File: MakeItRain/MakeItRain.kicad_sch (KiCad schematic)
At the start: 16 parts, among them IC1 MCP23008T-E_SS, J1 Conn_02x14_Odd_Even, J2 Conn_02x19_Odd_Even, J3 Conn_01x19, U1 MCP23008-xP

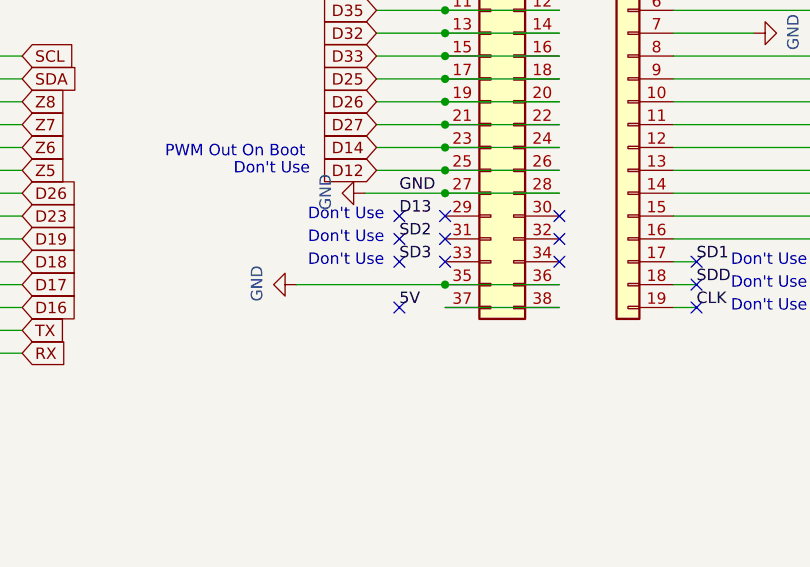
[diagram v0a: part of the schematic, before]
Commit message: in the process of cleaning up the HardwareValidation.ino and fixing a major fuck up for the board. misread a pin header.
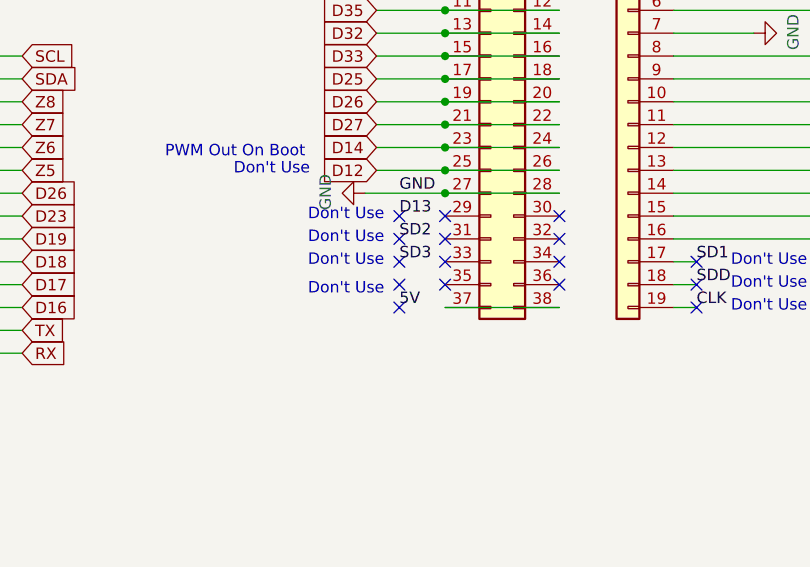
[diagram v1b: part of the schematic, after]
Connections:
- net GND: no longer J2.35 (Pin_35), J2.36 (Pin_36)
- no-connect marks 19 -> 22
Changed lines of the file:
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@@
 (kicad_sch (version 20211123) (generator eeschema)
   (paper "A4")
-  (junction (at 220.98 146.05) (diameter 0) (color 0 0 0 0)
-  )
   (junction (at 142.24 146.05) (diameter 0) (color 0 0 0 0)
   )
@@
   (no_connect (at 233.68 140.97))
   (no_connect (at 233.68 143.51))
+  (no_connect (at 215.9 146.05))
+  (no_connect (at 233.68 146.05))
   (no_connect (at 248.92 148.59))
+  (no_connect (at 220.98 146.05))
   (wire (pts (xy 90.17 142.875) (xy 92.71 142.875))
     (stroke (width 0) (type default) (color 0 0 0 0))
@@
     (stroke (width 0) (type default) (color 0 0 0 0))
   )
-  (wire (pts (xy 220.98 146.05) (xy 233.68 146.05))
-    (stroke (width 0) (type default) (color 0 0 0 0))
-  )
   (wire (pts (xy 90.17 125.095) (xy 92.71 125.095))
     (stroke (width 0) (type default) (color 0 0 0 0))
@@
   )
   (wire (pts (xy 233.68 107.95) (xy 220.98 107.95))
-    (stroke (width 0) (type default) (color 0 0 0 0))
-  )
-  (wire (pts (xy 204.47 146.05) (xy 220.98 146.05))
     (stroke (width 0) (type default) (color 0 0 0 0))
   )
@@
   )
   (text "Don't Use" (at 252.73 144.145 0)
+    (effects (font (size 1.27 1.27)) (justify left bottom))
+  )
+  (text "Don't Use" (at 205.74 147.32 0)
     (effects (font (size 1.27 1.27)) (justify left bottom))
   )
@@
     (pin "1")
   )
-  (symbol (lib_id "power:GND") (at 204.47 146.05 270) (mirror x) (unit 1)
-    (in_bom yes) (on_board yes)
-    (property "Reference" "#PWR0103" (id 0) (at 198.12 146.05 0)
-      (effects (font (size 1.27 1.27)) hide)
-    )
-    (property "Value" "GND" (id 1) (at 200.0758 145.923 0))
-    (property "Footprint" "" (id 2) (at 204.47 146.05 0)
-      (effects (font (size 1.27 1.27)) hide)
-    )
-    (property "Datasheet" "" (id 3) (at 204.47 146.05 0)
-      (effects (font (size 1.27 1.27)) hide)
-    )
-    (pin "1")
-  )
   (symbol (lib_id "Device:R") (at 35.56 116.84 0) (unit 1)
     (in_bom yes) (on_board yes)
@@
       (reference "#PWR0102") (unit 1) (value "+3.3V") (footprint "")
     )
-    (path "/45143e3f-fce8-46ca-878b-622ef7f7645d"
-      (reference "#PWR0103") (unit 1) (value "GND") (footprint "")
-    )
     (path "/681cdba4-7e5c-45e3-bb80-441c833d63d5"

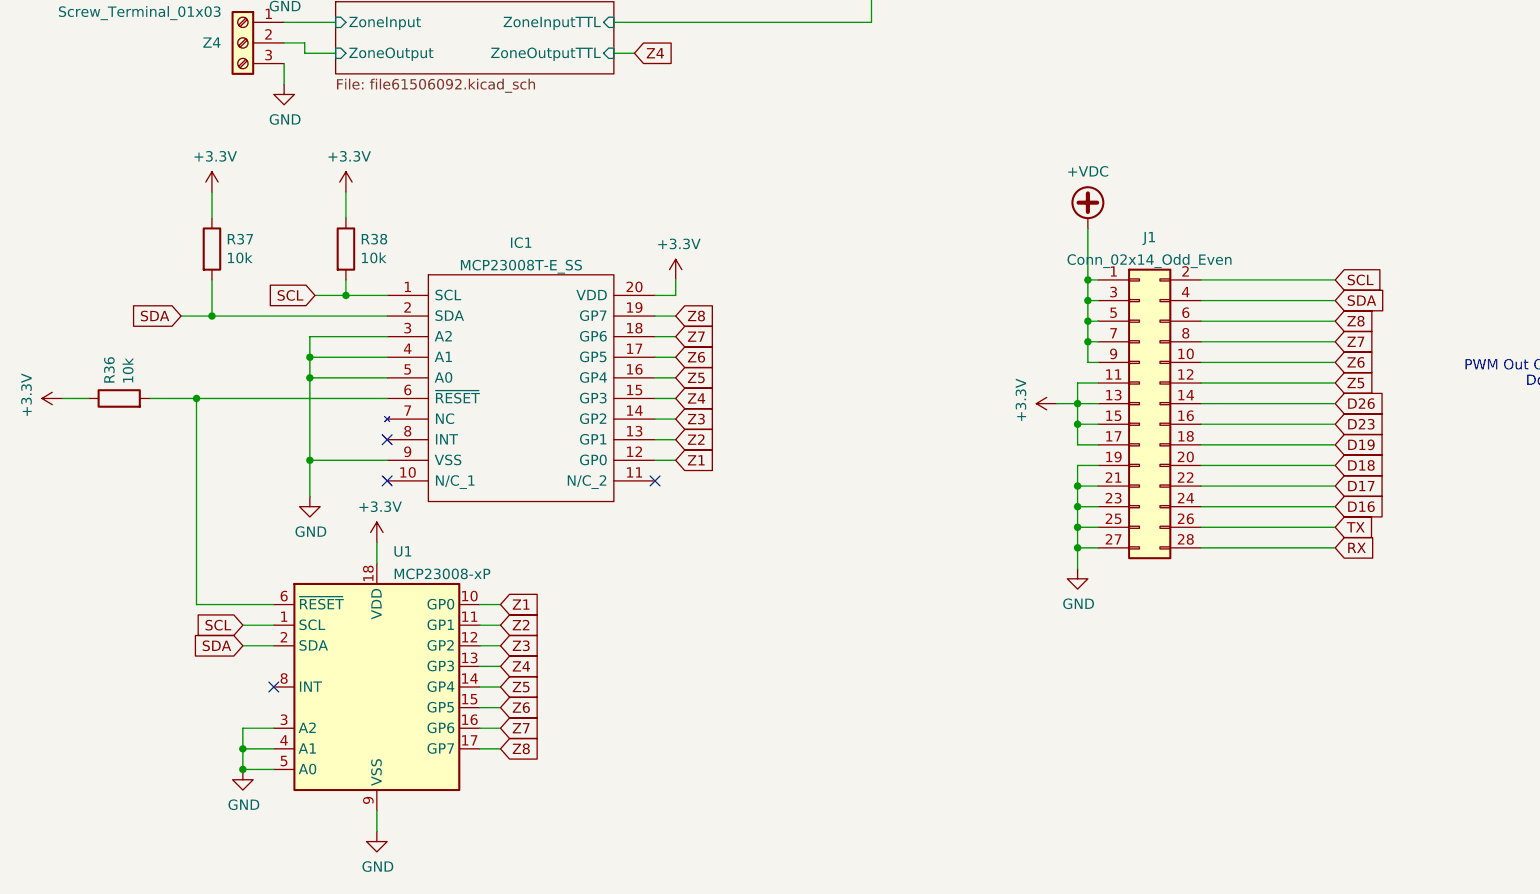
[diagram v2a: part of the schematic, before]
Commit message: WIP - Pre Re-Routing and other Tweaks.
* Removed SMD package for the MCP23008
* removed routings to fix the routes for I2C bus
* flipped rx/tx with SDA/SCL on the expansion port to make routing easier.
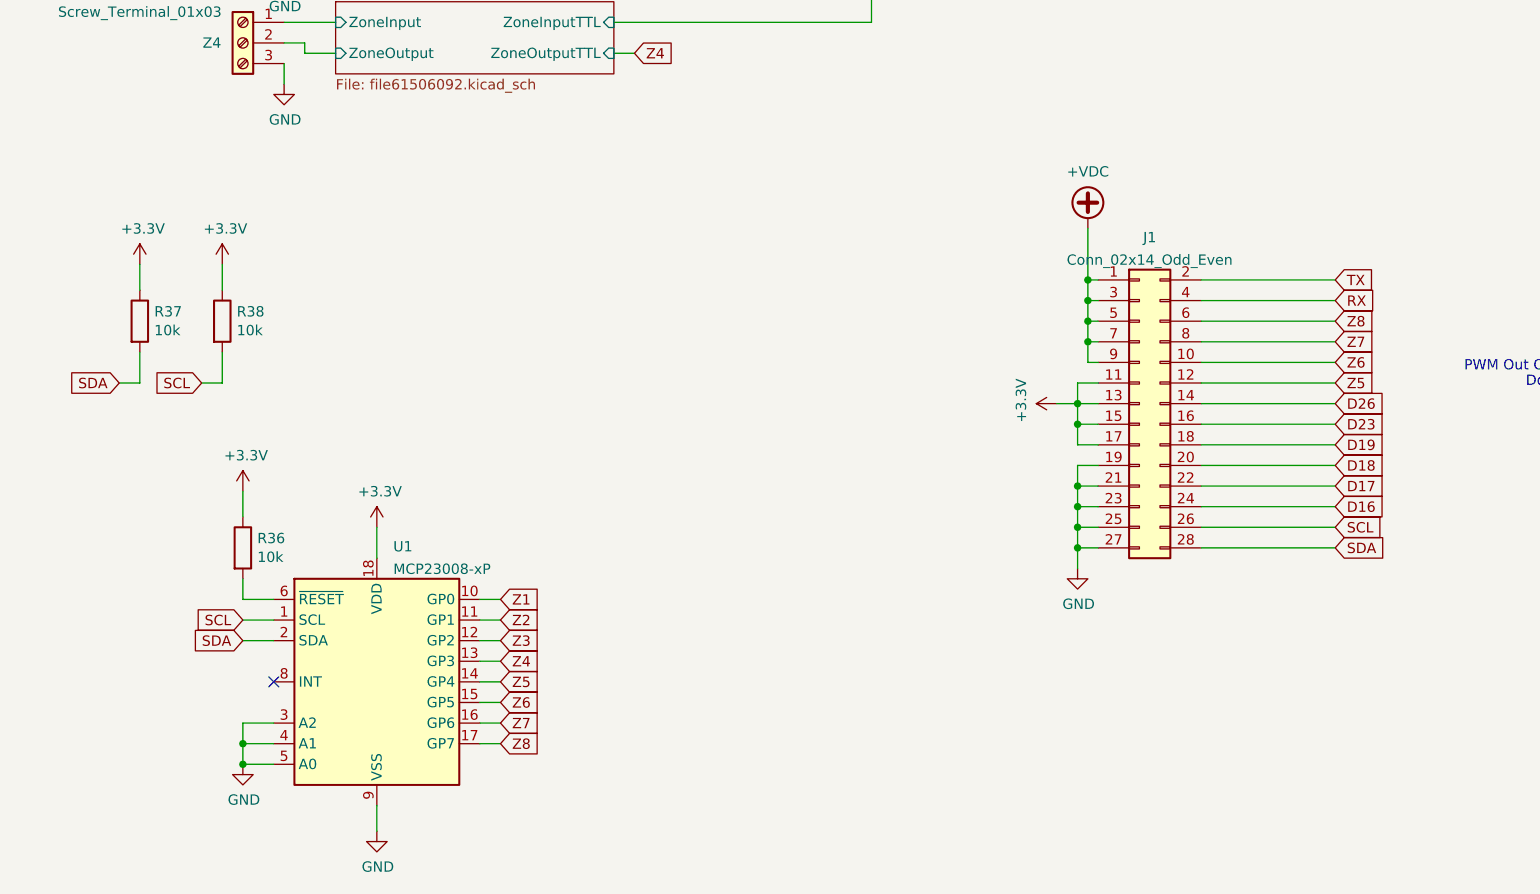
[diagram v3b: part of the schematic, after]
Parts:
- removed IC1: MCP23008T-E_SS, SOP65P780X200-20N, symbol Samac_Sys:MCP23008T-E_SS
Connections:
- net D21: now also J1.28 (Pin_28); no longer J1.4 (Pin_4)
- net D22: now also J1.26 (Pin_26); no longer J1.2 (Pin_2)
- net RX: now also J1.4 (Pin_4); no longer J1.28 (Pin_28)
- net TX: now also J1.2 (Pin_2); no longer J1.26 (Pin_26)
- no-connect marks 22 -> 19
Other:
- moved on the sheet: R36, R37, R38, U1

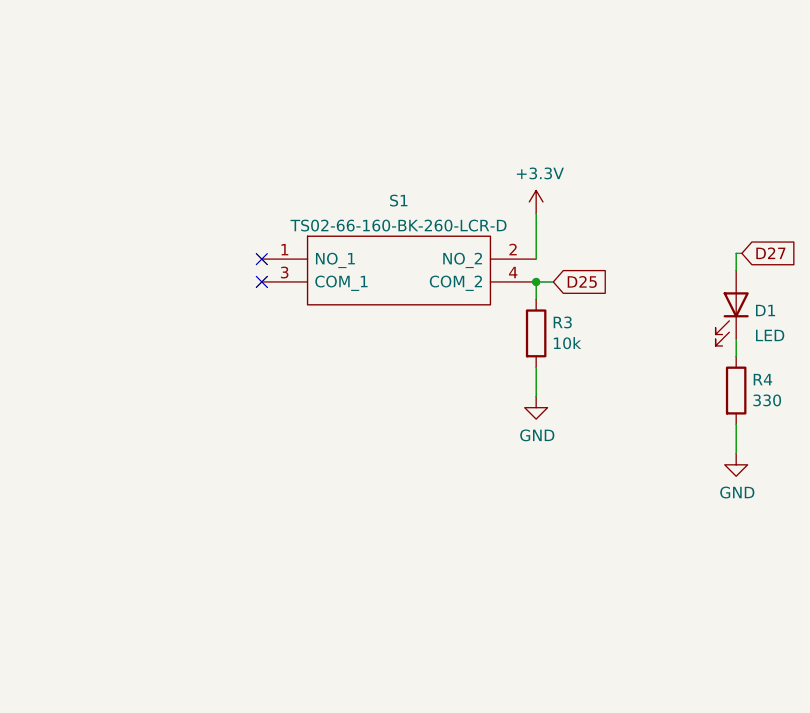
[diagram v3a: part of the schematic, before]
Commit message: MakeItRain * Main Board Fixed Routing. * replaced Opamp with the part that i can get as the old one is EOL * generated all the fab files i need. * updated the daughter plug witht eh i2c ttl flip * fixed I2C issues * DRC'ed the board
MakeItRain - DaughterBoard - Zone Expansion
* updated the daughter plug witht eh i2c ttl flip
* fixed some of the routings
* generated new fab files
* DRC'ed the board
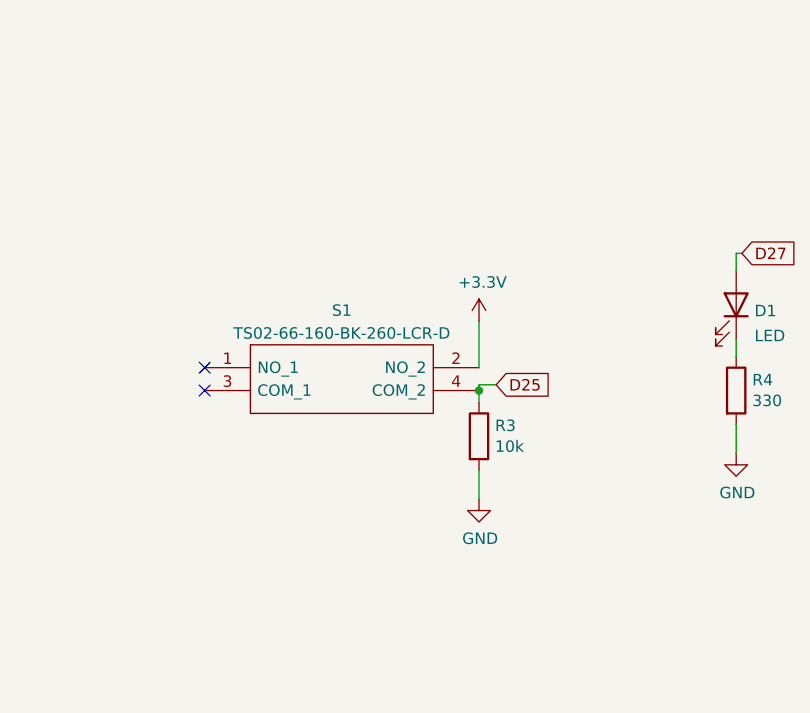
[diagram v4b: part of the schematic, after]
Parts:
- removed S1: TS02-66-160-BK-260-LCR-D, TS0266160BK260LCRD, symbol Samac_Sys:TS02-66-160-BK-260-LCR-D
- added S1: TS02-66-160-BK-260-LCR-D, TS0266160BK260LCRD, symbol SamacSys_Parts:TS02-66-160-BK-260-LCR-D
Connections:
- net +3V3: now also S1.2 (NO_2)
- net D25: now also S1.4 (COM_2)
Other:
- moved on the sheet: R3

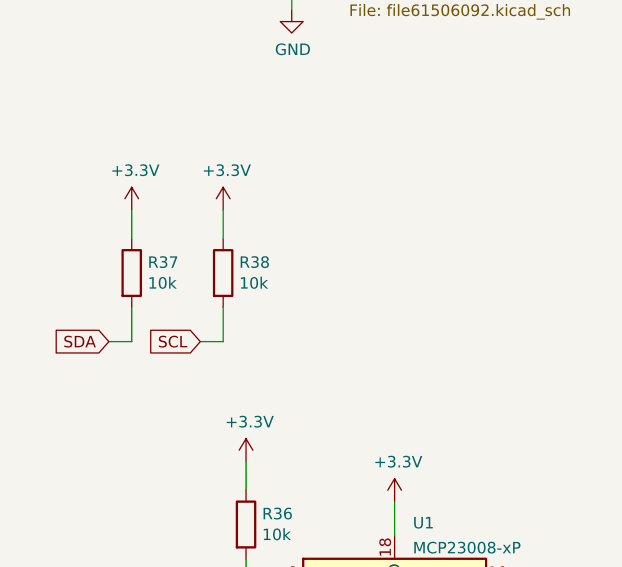
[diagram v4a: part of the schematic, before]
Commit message: Updating the I2C pullup resistor values to 2.2K * updated BOM/MakeItRain - Maine Board - Bom.xls * updated schematics and layout values * update ibom.html
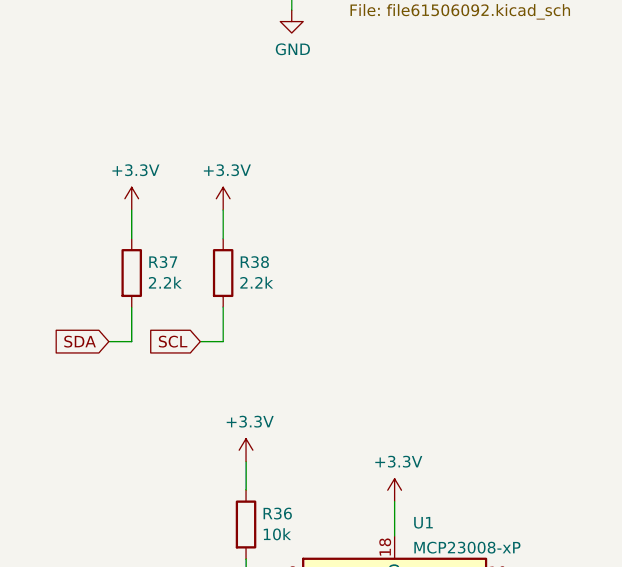
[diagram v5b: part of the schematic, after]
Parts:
- R37, R38: value 10k -> 2.2k
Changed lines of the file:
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@@
       (effects (font (size 1.27 1.27)) (justify left))
     )
-    (property "Value" "10k" (at 38.608 126.873 0)
+    (property "Value" "2.2k" (at 38.608 126.873 0)
       (effects (font (size 1.27 1.27)) (justify left))
     )
@@
       (effects (font (size 1.27 1.27)) (justify left))
     )
-    (property "Value" "10k" (at 28.448 126.873 0)
+    (property "Value" "2.2k" (at 28.448 126.873 0)
       (effects (font (size 1.27 1.27)) (justify left))
     )

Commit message: imput redesign
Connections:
- net Zone1IO/ZoneInput is gone; now on net InputIsolation/1in: Z1.1 (Pin_1)
- net Zone2IO/ZoneInput is gone; now on net InputIsolation/2in: Z2.1 (Pin_1)
- net Zone3IO/ZoneInput is gone; now on net InputIsolation/3in: Z3.1 (Pin_1)
- net Zone4IO/ZoneInput is gone; now on net InputIsolation/4in: Z4.1 (Pin_1)
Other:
- sheet Zone1IO ports: added none; removed ZoneInput, ZoneInputTTL
- sheet Zone2IO ports: added none; removed ZoneInput, ZoneInputTTL
- sheet Zone3IO ports: added none; removed ZoneInput, ZoneInputTTL
- sheet Zone4IO ports: added none; removed ZoneInput, ZoneInputTTL
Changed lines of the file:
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@@
-    (stroke (width 0) (type default))
-  )
-  (wire (pts (xy 44.45 88.9) (xy 50.8 88.9))
     (stroke (width 0) (type default))
   )
@@
     (stroke (width 0) (type default))
   )
-  (wire (pts (xy 85.09 46.99) (xy 121.92 46.99))
-    (stroke (width 0) (type default))
-  )
   (wire (pts (xy 233.68 107.95) (xy 220.98 107.95))
     (stroke (width 0) (type default))
@@
     (stroke (width 0) (type default))
   )
-  (wire (pts (xy 85.09 74.93) (xy 124.46 74.93))
-    (stroke (width 0) (type default))
-  )
   (wire (pts (xy 157.48 153.67) (xy 173.99 153.67))
     (stroke (width 0) (type default))
@@
     (stroke (width 0) (type default))
   )
-  (wire (pts (xy 116.84 88.9) (xy 85.09 88.9))
+  (wire (pts (xy 44.45 88.9) (xy 116.84 88.9))
     (stroke (width 0) (type default))
   )
@@
     (stroke (width 0) (type default))
   )
+  (wire (pts (xy 44.45 46.99) (xy 121.92 46.99))
+    (stroke (width 0) (type default))
+  )
   (wire (pts (xy 246.38 125.73) (xy 261.62 125.73))
     (stroke (width 0) (type default))
@@
     (stroke (width 0) (type default))
   )
-  (wire (pts (xy 44.45 46.99) (xy 50.8 46.99))
-    (stroke (width 0) (type default))
-  )
   (wire (pts (xy 142.24 151.13) (xy 144.78 151.13))
     (stroke (width 0) (type default))
@@
     (stroke (width 0) (type default))
   )
-  (wire (pts (xy 50.8 60.96) (xy 44.45 60.96))
+  (wire (pts (xy 44.45 60.96) (xy 116.84 60.96))
     (stroke (width 0) (type default))
   )
@@
     (stroke (width 0) (type default))
   )
-  (wire (pts (xy 44.45 74.93) (xy 50.8 74.93))
+  (wire (pts (xy 44.45 74.93) (xy 124.46 74.93))
     (stroke (width 0) (type default))
   )
@@
   )
   (wire (pts (xy 213.36 107.95) (xy 220.98 107.95))
-    (stroke (width 0) (type default))
-  )
-  (wire (pts (xy 116.84 60.96) (xy 85.09 60.96))
     (stroke (width 0) (type default))
   )
@@
     )
   )
-  (sheet (at 50.8 44.45) (size 34.29 8.89) (fields_autoplaced)
+  (sheet (at 50.8 48.26) (size 34.29 5.08) (fields_autoplaced)
     (stroke (width 0) (type solid))
     (fill (color 0 0 0 0.0000))
-    (property "Sheetname" "Zone1IO" (at 50.8 43.7384 0)
+    (property "Sheetname" "Zone1IO" (at 50.8 47.5484 0)
       (effects (font (size 1.27 1.27)) (justify left bottom))
     )
@@
       (effects (font (size 1.27 1.27)) (justify left top))
     )
-    (pin "ZoneInput" input (at 50.8 46.99 180)
-      (effects (font (size 1.27 1.27)) (justify left))
-    )
-    (pin "ZoneInputTTL" input (at 85.09 46.99 0)
-      (effects (font (size 1.27 1.27)) (justify right))
-    )
     (pin "ZoneOutputTTL" input (at 85.09 50.8 0)
       (effects (font (size 1.27 1.27)) (justify right))
@@
     )
   )
-  (sheet (at 50.8 58.42) (size 34.29 8.89) (fields_autoplaced)
+  (sheet (at 50.8 63.5) (size 34.29 3.81) (fields_autoplaced)
     (stroke (width 0) (type solid))
     (fill (color 0 0 0 0.0000))
-    (property "Sheetname" "Zone2IO" (at 50.8 57.7084 0)
+    (property "Sheetname" "Zone2IO" (at 50.8 62.7884 0)
       (effects (font (size 1.27 1.27)) (justify left bottom))
     )
@@
       (effects (font (size 1.27 1.27)) (justify left top))
     )
-    (pin "ZoneInput" input (at 50.8 60.96 180)
-      (effects (font (size 1.27 1.27)) (justify left))
-    )
-    (pin "ZoneInputTTL" input (at 85.09 60.96 0)
-      (effects (font (size 1.27 1.27)) (justify right))
-    )
     (pin "ZoneOutputTTL" input (at 85.09 64.77 0)
       (effects (font (size 1.27 1.27)) (justify right))
@@
     )
   )
-  (sheet (at 50.8 72.39) (size 34.29 8.89) (fields_autoplaced)
+  (sheet (at 50.8 76.2) (size 34.29 5.08) (fields_autoplaced)
     (stroke (width 0) (type solid))
     (fill (color 0 0 0 0.0000))
-    (property "Sheetname" "Zone3IO" (at 50.8 71.6784 0)
+    (property "Sheetname" "Zone3IO" (at 50.8 75.4884 0)
       (effects (font (size 1.27 1.27)) (justify left bottom))
     )
@@
       (effects (font (size 1.27 1.27)) (justify left top))
     )
-    (pin "ZoneInput" input (at 50.8 74.93 180)
-      (effects (font (size 1.27 1.27)) (justify left))
-    )
-    (pin "ZoneInputTTL" input (at 85.09 74.93 0)
-      (effects (font (size 1.27 1.27)) (justify right))
-    )
     (pin "ZoneOutputTTL" input (at 85.09 78.74 0)
       (effects (font (size 1.27 1.27)) (justify right))
@@
     )
   )
-  (sheet (at 50.8 86.36) (size 34.29 8.89) (fields_autoplaced)
+  (sheet (at 50.8 90.17) (size 34.29 5.08) (fields_autoplaced)
     (stroke (width 0) (type solid))
     (fill (color 0 0 0 0.0000))
-    (property "Sheetname" "Zone4IO" (at 50.8 85.6484 0)
+    (property "Sheetname" "Zone4IO" (at 50.8 89.4584 0)
       (effects (font (size 1.27 1.27)) (justify left bottom))
     )
@@
       (effects (font (size 1.27 1.27)) (justify left top))
     )
-    (pin "ZoneInput" input (at 50.8 88.9 180)
-      (effects (font (size 1.27 1.27)) (justify left))
-    )
-    (pin "ZoneInputTTL" input (at 85.09 88.9 0)
-      (effects (font (size 1.27 1.27)) (justify right))
-    )
     (pin "ZoneOutputTTL" input (at 85.09 92.71 0)
